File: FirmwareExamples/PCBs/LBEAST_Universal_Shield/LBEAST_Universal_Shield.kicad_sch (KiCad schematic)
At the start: 53 parts, among them J1 MTJ-883X1, J10 CAN BUS, J11 JST-XH 2-Pin Fan, J2 MTJ-883X1, J3 MTJ-883X1, J4 MTJ-883X1, J5 MTJ-883X1, J6 MTJ-883X1, J7 MTJ-883X1, J8 MTJ-883X1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

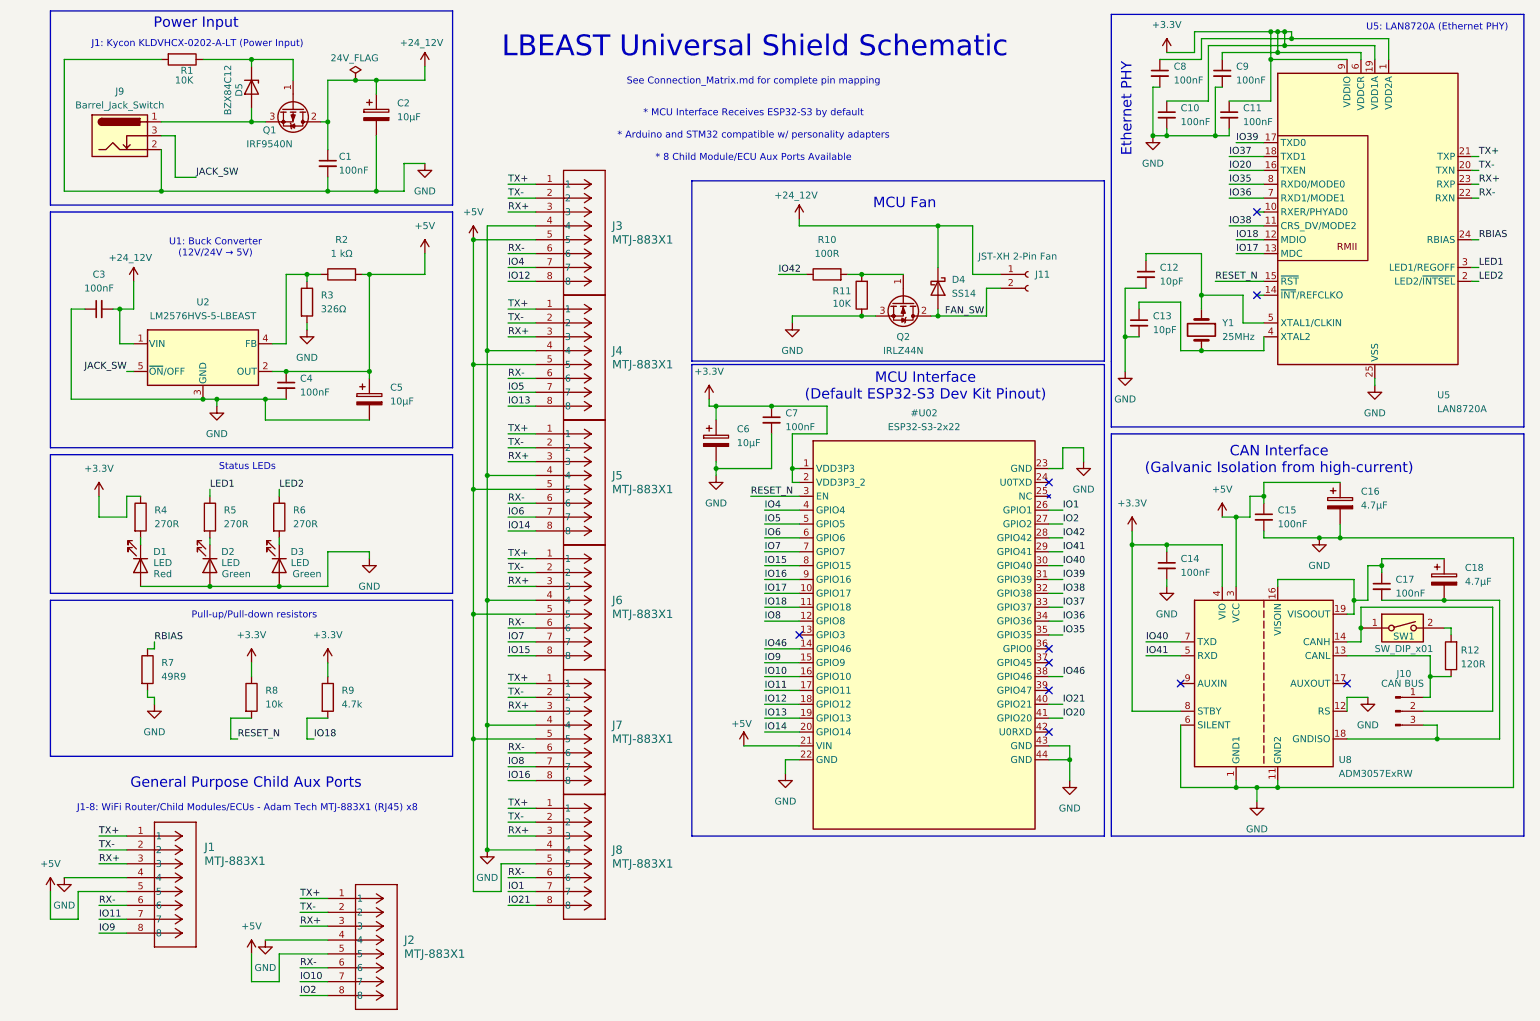
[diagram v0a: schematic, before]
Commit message: complete alpha Universal Shield PCB
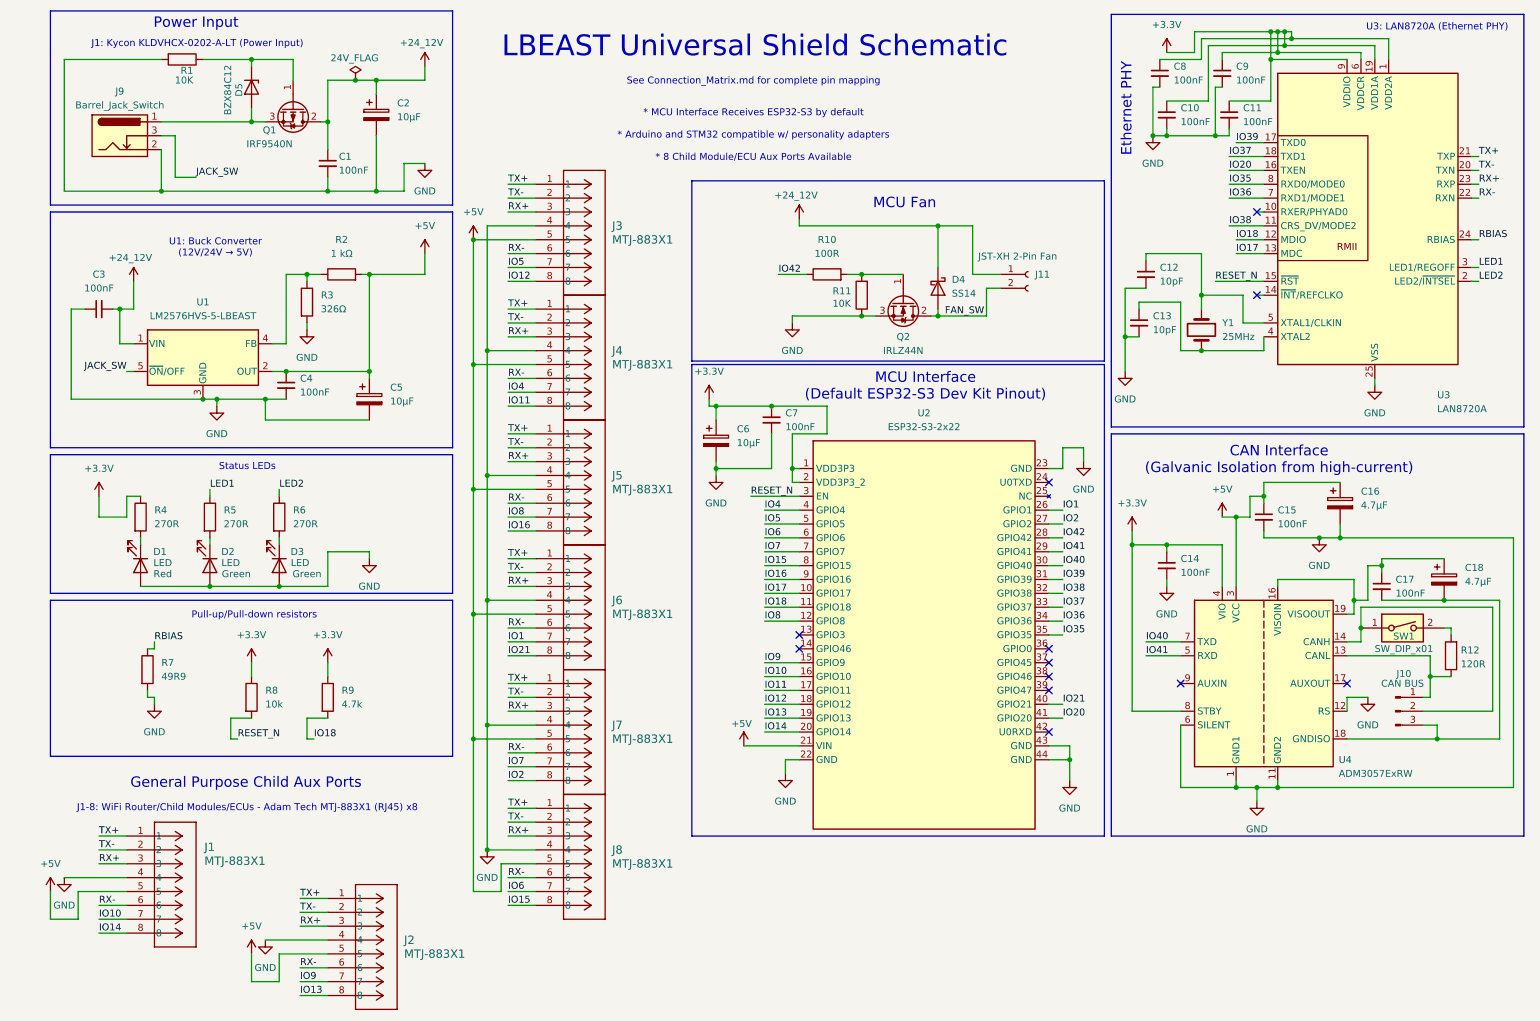
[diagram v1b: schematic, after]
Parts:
- added U2: ESP32-S3-2x22, LBEASTLibrary:ESP32-S3_2x22_Header_v3, symbol ESP32-S3-2x22:ESP32-S3-2x22
- SW1: footprint (none) -> Button_Switch_SMD:SW_DIP_SPSTx01_Slide_6.7x4.1mm_W6.73mm_P2.54mm_LowProfile_JPin
- renumbered U2 to U1, U5 to U3, U8 to U4
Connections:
- net +3.3V: now also U2.1 (VDD3P3), U2.2 (VDD3P3_2)
- net +5V: now also U2.21 (VIN)
- net IO1: now also J6.7, U2.26 (GPIO1); no longer J8.7
- net IO10: now also J1.7, U2.16 (GPIO10); no longer J2.7
- net IO11: now also J4.8, U2.17 (GPIO11); no longer J1.7
- net IO12: now also U2.18 (GPIO12)
- net IO13: now also J2.8, U2.19 (GPIO13); no longer J4.8
- net IO14: now also J1.8, U2.20 (GPIO14); no longer J5.8
- net IO15: now also J8.8, U2.8 (GPIO15); no longer J6.8
- net IO16: now also J5.8, U2.9 (GPIO16); no longer J7.8
- net IO17: now also U2.10 (GPIO17)
- net IO18: now also U2.11 (GPIO18)
- net IO2: now also J7.8, U2.27 (GPIO2); no longer J2.8
- net IO20: now also U2.41 (GPIO20)
- net IO21: now also J6.8, U2.40 (GPIO21); no longer J8.8
- net IO35: now also U2.35 (GPIO35)
- net IO36: now also U2.34 (GPIO36)
- net IO37: now also U2.33 (GPIO37)
- net IO38: now also U2.32 (GPIO38)
- net IO39: now also U2.31 (GPIO39)
- net IO4: now also J4.7, U2.4 (GPIO4); no longer J3.7
- net IO40: now also U2.30 (GPIO40)
- net IO41: now also U2.29 (GPIO41)
- net IO42: now also U2.28 (GPIO42)
- net IO5: now also J3.7, U2.5 (GPIO5); no longer J4.7
- net IO6: now also J8.7, U2.6 (GPIO6); no longer J5.7
- net IO7: now also J7.7, U2.7 (GPIO7); no longer J6.7
- net IO8: now also J5.7, U2.12 (GPIO8); no longer J7.7
- net IO9: now also J2.7, U2.15 (GPIO9); no longer J1.8
- net RESET_N: now also U2.3 (EN)
- net ESP32-S3-2x22 renamed GND
- net GND: now also U2.22 (GND), U2.23 (GND), U2.43 (GND), U2.44 (GND)
- no-connect marks 10 -> 12
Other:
- note added: "U3: LAN8720A (Ethernet PHY)"
- note removed: "U5: LAN8720A (Ethernet PHY)"
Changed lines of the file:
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@@
 		)
 	)
-	(text "U5: LAN8720A (Ethernet PHY)"
+	(text "U3: LAN8720A (Ethernet PHY)"
 		(exclude_from_sim no)
 		(at 267.97 17.018 0)
@@
 	)
 	(no_connect
+		(at 151.13 130.81)
+	)
+	(no_connect
 		(at 251.46 137.16)
 	)
@@
 	)
 	(no_connect
+		(at 196.85 135.89)
+	)
+	(no_connect
 		(at 196.85 146.05)
 	)
@@
 	(wire
 		(pts
-			(xy 196.85 135.89) (xy 199.39 135.89)
-		)
-		(stroke
-			(width 0)
-			(type default)
-		)
-	)
-	(wire
-		(pts
 			(xy 97.79 162.56) (xy 102.87 162.56)
 		)
@@
 	(wire
 		(pts
-			(xy 144.78 130.81) (xy 151.13 130.81)
-		)
-		(stroke
-			(width 0)
-			(type default)
-		)
-	)
-	(wire
-		(pts
 			(xy 203.2 93.98) (xy 203.2 96.52)
 		)
@@
 		)
 	)
-	(label "IO46"
-		(at 199.39 135.89 0)
-		(effects
-			(font
-				(size 1.27 1.27)
-			)
-			(justify left bottom)
-		)
-	)
-	(label "IO13"
+	(label "IO11"
 		(at 97.79 86.36 0)
 		(effects
@@
 		)
 	)
-	(label "IO5"
+	(label "IO4"
 		(at 97.79 83.82 0)
 		(effects
@@
 		)
 	)
-	(label "IO10"
+	(label "IO9"
 		(at 59.69 191.77 0)
 		(effects
@@
 		)
 	)
-	(label "IO8"
+	(label "IO7"
 		(at 97.79 152.4 0)
 		(effects
@@
 		)
 	)
-	(label "IO4"
+	(label "IO5"
 		(at 97.79 60.96 0)
 		(effects
@@
 		)
 	)
-	(label "IO21"
+	(label "IO15"
 		(at 97.79 177.8 0)
 		(effects
@@
 		)
 	)
-	(label "IO11"
+	(label "IO10"
 		(at 22.86 180.34 0)
 		(effects
@@
 		)
 	)
-	(label "IO14"
+	(label "IO16"
 		(at 97.79 109.22 0)
 		(effects
@@
 		)
 	)
-	(label "IO9"
+	(label "IO14"
 		(at 22.86 182.88 0)
 		(effects
@@
 		)
 	)
-	(label "IO1"
+	(label "IO6"
 		(at 97.79 175.26 0)
 		(effects
@@
 		)
 	)
-	(label "IO7"
+	(label "IO1"
 		(at 97.79 129.54 0)
 		(effects
@@
 		)
 	)
-	(label "IO15"
+	(label "IO21"
 		(at 97.79 132.08 0)
 		(effects
@@
 		)
 	)
-	(label "IO16"
+	(label "IO2"
 		(at 97.79 154.94 0)
 		(effects
@@
 		)
 	)
-	(label "IO46"
-		(at 144.78 130.81 0)
-		(effects
-			(font
-				(size 1.27 1.27)
-			)
-			(justify left bottom)
-		)
-	)
-	(label "IO2"
+	(label "IO13"
 		(at 59.69 194.31 0)
 		(effects
@@
 		)
 	)
-	(label "IO6"
+	(label "IO8"
 		(at 97.79 106.68 0)
 		(effects
@@
 		(on_board yes)
 		(dnp no)
-		(property "Reference" "U5"
+		(property "Reference" "U3"
 			(at 267.97 84.328 0)
 			(effects
@@
 			(project ""
 				(path "/67960650-84cc-4502-bcc3-41421fb0fa99"
-					(reference "U5")
+					(reference "U3")
 					(unit 1)
 				)
@@
 			)
 		)
-		(property "Footprint" ""
+		(property "Footprint" "Button_Switch_SMD:SW_DIP_SPSTx01_Slide_6.7x4.1mm_W6.73mm_P2.54mm_LowProfile_JPin"
 			(at 261.62 127 0)
 			(effects
@@
 		(dnp no)
 		(fields_autoplaced yes)
-		(property "Reference" "U2"
+		(property "Reference" "U1"
 			(at 41.91 67.31 0)
 			(effects
@@
 			(project ""
 				(path "/67960650-84cc-4502-bcc3-41421fb0fa99"
-					(reference "U2")
+					(reference "U1")
 					(unit 1)
 				)
@@
 		(on_board yes)
 		(dnp no)
-		(property "Reference" "U8"
+		(property "Reference" "U4"
 			(at 249.936 151.13 0)
 			(effects
@@
 			(project ""
 				(path "/67960650-84cc-4502-bcc3-41421fb0fa99"
-					(reference "U8")
+					(reference "U4")
 					(unit 1)
 				)
@@
 		(dnp no)
 		(fields_autoplaced yes)
-		(property "Reference" "#U02"
+		(property "Reference" "U2"
 			(at 173.99 87.63 0)
 			(effects
@@
 			)
 		)
-		(property "Footprint" "LBEASTLibrary:ESP32-S3_2x22_Header"
+		(property "Footprint" "LBEASTLibrary:ESP32-S3_2x22_Header_v3"
 			(at 173.99 176.53 0)
 			(effects
@@
 			(project ""
 				(path "/67960650-84cc-4502-bcc3-41421fb0fa99"
-					(reference "#U02")
+					(reference "U2")
 					(unit 1)
 				)

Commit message: add power differential protection to LBUS aux ports
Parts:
- added D1, D2, D3, D4, D5, D6, D7, D8: MBR735, Package_TO_SOT_THT:TO-220-2_Vertical, symbol Diode:MBR735
- added J12: UART_Debug_Header, Connector_PinHeader_2.54mm:PinHeader_1x04_P2.54mm_Vertical, symbol Connector:Conn_01x04_Pin
- added SW2: J1_PWR_SW, Button_Switch_SMD:SW_DIP_SPSTx01_Slide_6.7x4.1mm_W6.73mm_P2.54mm_LowProfile_JPin, symbol Switch:SW_DIP_x01
- added SW3: J2_PWR_SW, Button_Switch_SMD:SW_DIP_SPSTx01_Slide_6.7x4.1mm_W6.73mm_P2.54mm_LowProfile_JPin, symbol Switch:SW_DIP_x01
- added SW4: J3_PWR_SW, Button_Switch_SMD:SW_DIP_SPSTx01_Slide_6.7x4.1mm_W6.73mm_P2.54mm_LowProfile_JPin, symbol Switch:SW_DIP_x01
- added SW5: J4_PWR_SW, Button_Switch_SMD:SW_DIP_SPSTx01_Slide_6.7x4.1mm_W6.73mm_P2.54mm_LowProfile_JPin, symbol Switch:SW_DIP_x01
- added SW6: J5_PWR_SW, Button_Switch_SMD:SW_DIP_SPSTx01_Slide_6.7x4.1mm_W6.73mm_P2.54mm_LowProfile_JPin, symbol Switch:SW_DIP_x01
- added SW7: J6_PWR_SW, Button_Switch_SMD:SW_DIP_SPSTx01_Slide_6.7x4.1mm_W6.73mm_P2.54mm_LowProfile_JPin, symbol Switch:SW_DIP_x01
- added SW8: J7_PWR_SW, Button_Switch_SMD:SW_DIP_SPSTx01_Slide_6.7x4.1mm_W6.73mm_P2.54mm_LowProfile_JPin, symbol Switch:SW_DIP_x01
- added SW9: J8_PWR_SW, Button_Switch_SMD:SW_DIP_SPSTx01_Slide_6.7x4.1mm_W6.73mm_P2.54mm_LowProfile_JPin, symbol Switch:SW_DIP_x01
- renumbered D1 to D10, D2 to D11, D3 to D12, D4 to D13, D5 to D9
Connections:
- net +3.3V: now also J12.2 (Pin_2)
- net +5V: now also SW2.1, SW3.1, SW4.1, SW5.1, SW6.1, SW7.1, SW8.1, SW9.1; no longer J1.5, J2.5, J3.5, J4.5, J5.5, J6.5, J7.5, J8.5
- net GND: now also J12.1 (Pin_1)
- net IO24: now reaches U2.24 (U0TXD)
- net IO24: now also J12.4 (Pin_4)
- net IO44: now reaches U2.42 (U0RXD)
- net IO44: now also J12.3 (Pin_3)
- new net: D2.1 (K), J2.5
- new net: D6.2 (A), SW7.2
- new net: D5.2 (A), SW6.2
- new net: D4.1 (K), J4.5
- new net: D4.2 (A), SW5.2
- new net: D7.1 (K), J7.5
- new net: D6.1 (K), J6.5
- new net: D8.2 (A), SW9.2
- new net: D1.1 (K), J1.5
- new net: D1.2 (A), SW2.2
- new net: D3.1 (K), J3.5
- new net: D3.2 (A), SW4.2
- new net: D7.2 (A), SW8.2
- new net: D2.2 (A), SW3.2
- new net: D8.1 (K), J8.5
- new net: D5.1 (K), J5.5
- no-connect marks 12 -> 10
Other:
- note added: "Debug Breakout"
- moved on the sheet: J1, J2, J3, J4, J5, J6, J7, J8
